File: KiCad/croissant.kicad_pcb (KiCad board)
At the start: 2 copper layers, 32 x 23 mm, 7 parts, among them J1 USB_C_Receptacle, U1 LMC555xM

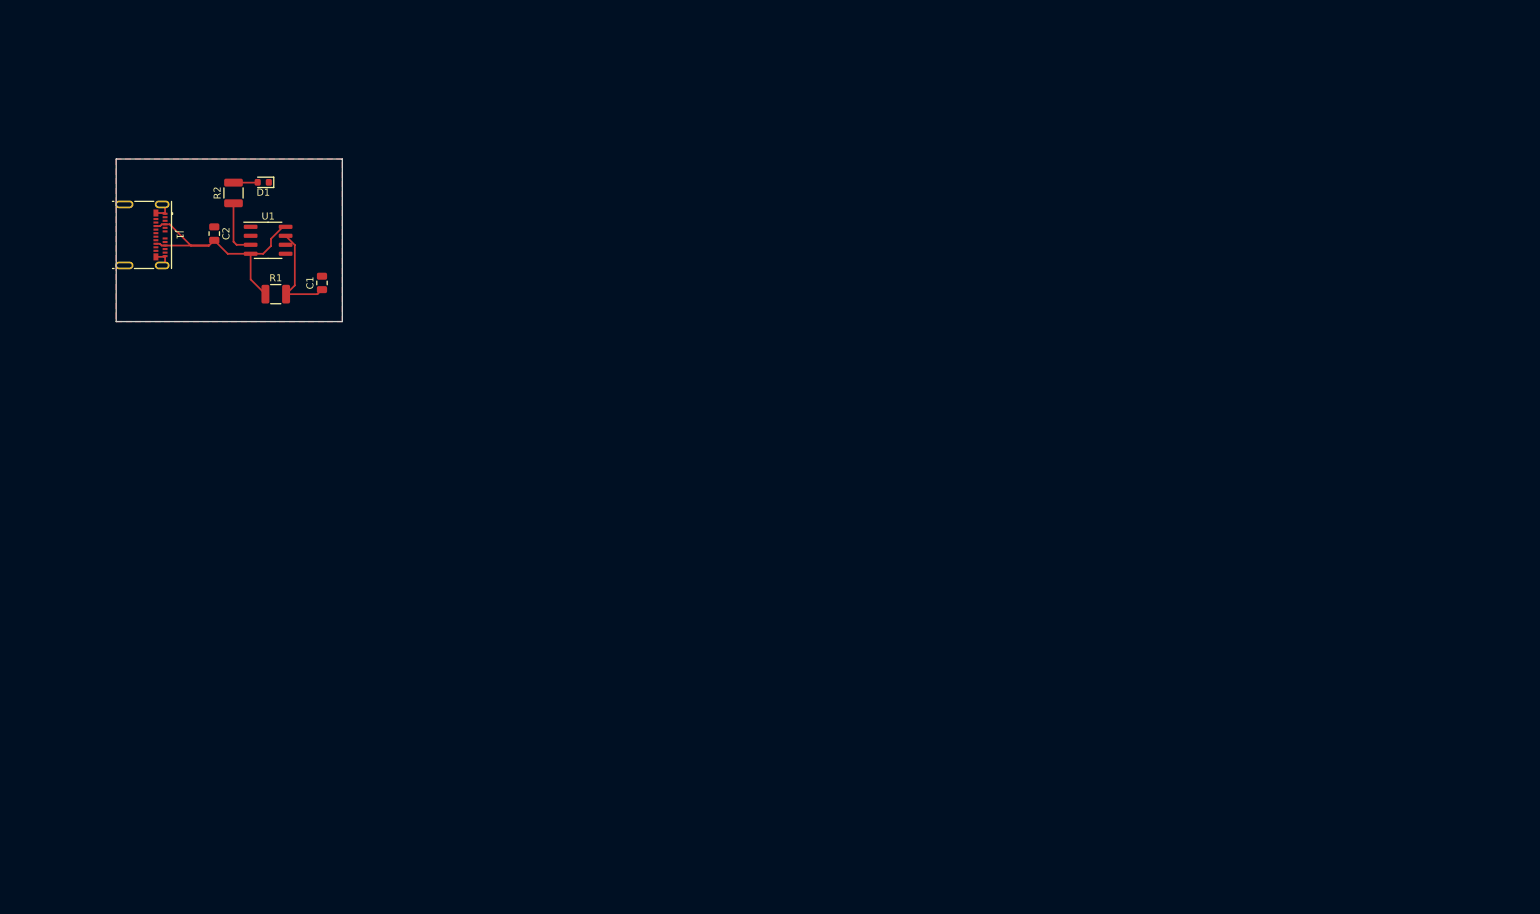
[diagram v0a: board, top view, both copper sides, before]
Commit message: Add board outline
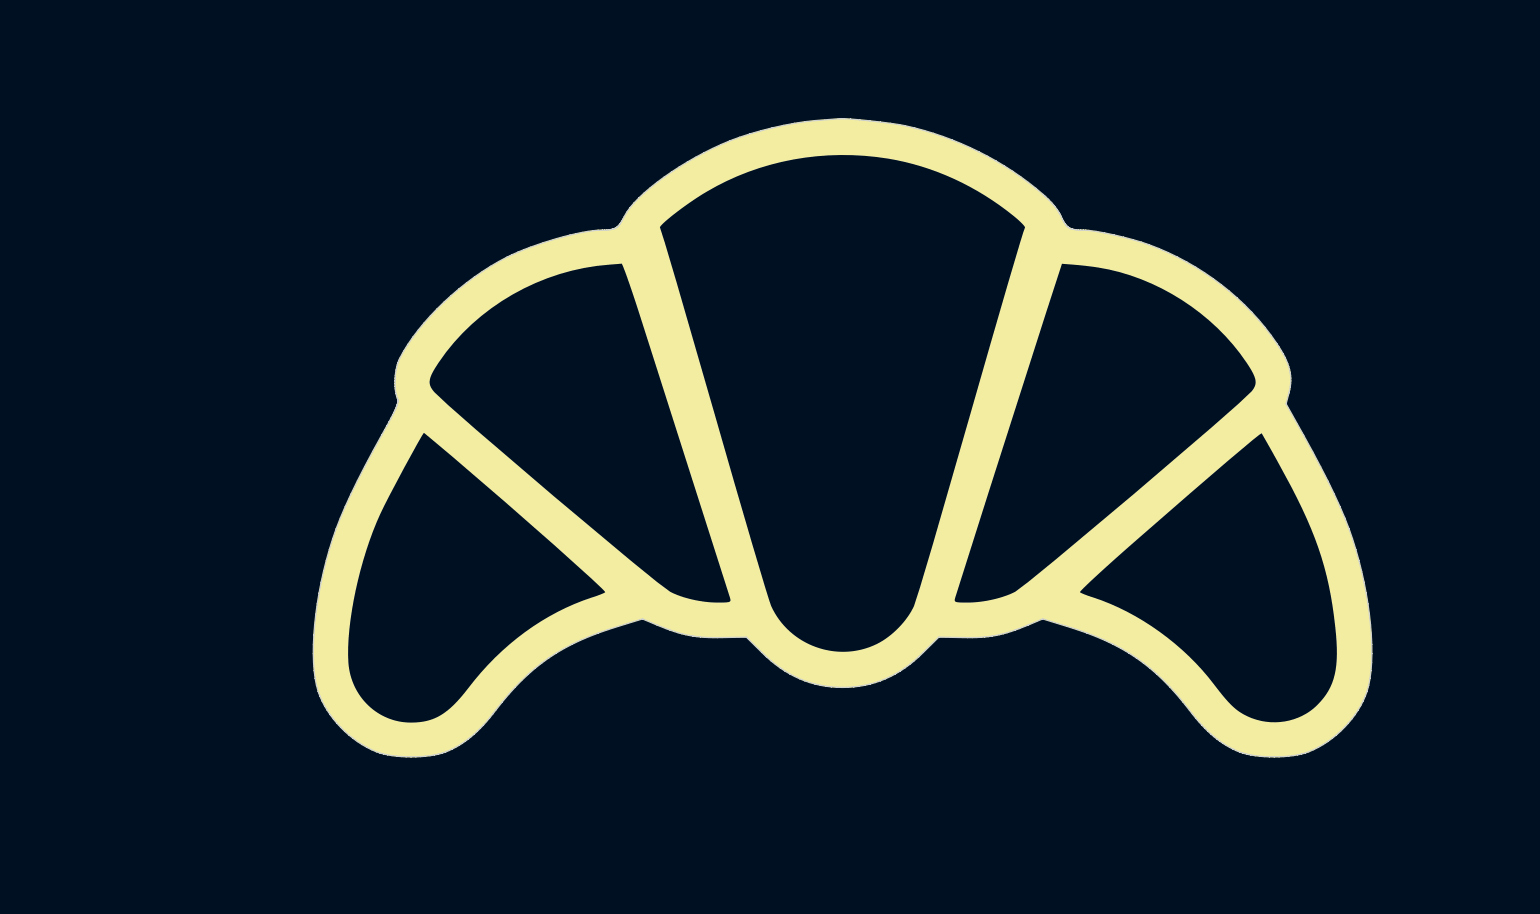
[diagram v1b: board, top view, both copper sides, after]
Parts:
- removed C1, C2: C, Capacitor_SMD:C_0805_2012Metric
- removed D1: LED, LED_SMD:LED_0603_1608Metric
- removed J1: USB_C_Receptacle, Connector_USB:USB_C_Receptacle_Molex_105450-0101
- removed R1, R2: R, Resistor_SMD:R_1210_3225Metric
- removed U1: LMC555xM, Package_SO:SOIC-8_3.9x4.9mm_P1.27mm
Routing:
- net +5V: track 37.2 -> 0.00 mm
- net Net-(U1-DIS): track 14.7 -> 0.00 mm
- net /555_output: track 8.04 -> 0.00 mm
- net GND: track 5.66 -> 0.00 mm
- net Net-(D1-A): track 3.44 -> 0.00 mm
- removed copper zone on F.Cu, net GND
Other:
- board size 32 x 23 mm -> 149.8 x 90.3 mm

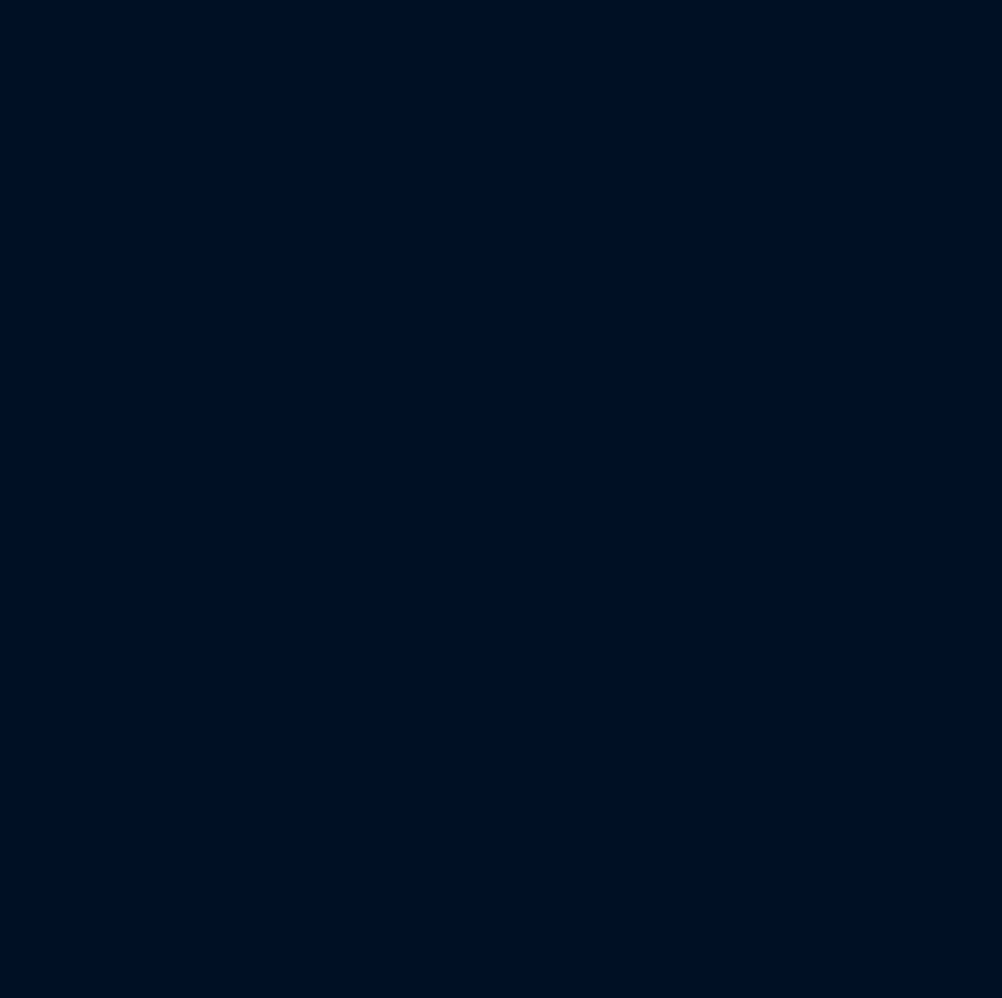
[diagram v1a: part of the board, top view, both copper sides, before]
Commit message: Fix footprints
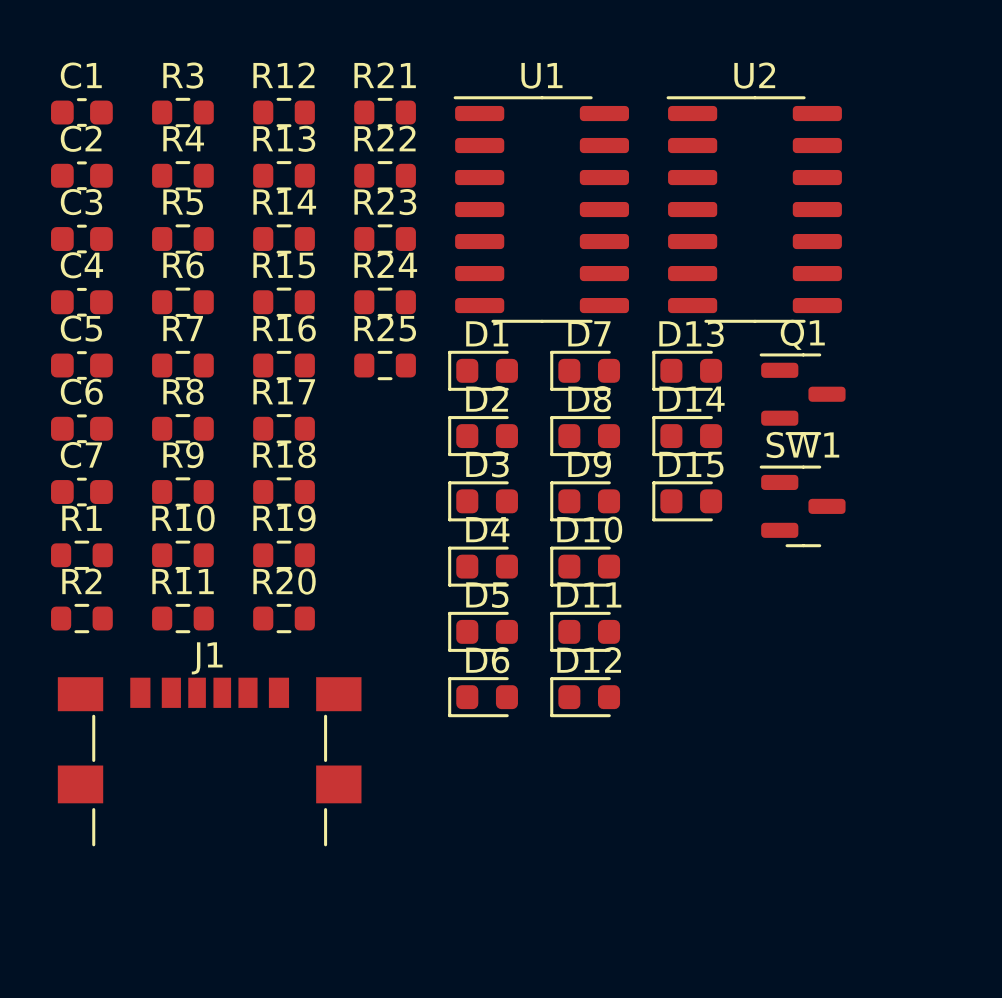
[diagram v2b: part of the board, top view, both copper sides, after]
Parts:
- added C1: C, Capacitor_SMD:C_0603_1608Metric, F.Cu at (51.7, 35.2)
- added C2: 22n, Capacitor_SMD:C_0603_1608Metric, F.Cu at (51.7, 37.7)
- added C3: 0.1u, Capacitor_SMD:C_0603_1608Metric, F.Cu at (51.7, 40.2)
- added C4: 0.1u, Capacitor_SMD:C_0603_1608Metric, F.Cu at (51.7, 42.7)
- added C5: 5n, Capacitor_SMD:C_0603_1608Metric, F.Cu at (51.7, 45.2)
- added C6: 1u, Capacitor_SMD:C_0603_1608Metric, F.Cu at (51.7, 47.7)
- added C7: 0.1u, Capacitor_SMD:C_0603_1608Metric, F.Cu at (51.7, 50.2)
- added D1: LED, LED_SMD:LED_0603_1608Metric, F.Cu at (67.8, 45.4)
- added D10: LED, LED_SMD:LED_0603_1608Metric, F.Cu at (71.8, 53.2)
- added D11: LED, LED_SMD:LED_0603_1608Metric, F.Cu at (71.8, 55.8)
- added D12: LED, LED_SMD:LED_0603_1608Metric, F.Cu at (71.8, 58.4)
- added D13: LED, LED_SMD:LED_0603_1608Metric, F.Cu at (75.9, 45.4)
- added D14: LED, LED_SMD:LED_0603_1608Metric, F.Cu at (75.9, 48.0)
- added D15: LED, LED_SMD:LED_0603_1608Metric, F.Cu at (75.9, 50.6)
- added D2: LED, LED_SMD:LED_0603_1608Metric, F.Cu at (67.8, 48.0)
- added D3: LED, LED_SMD:LED_0603_1608Metric, F.Cu at (67.8, 50.6)
- added D4: LED, LED_SMD:LED_0603_1608Metric, F.Cu at (67.8, 53.2)
- added D5: LED, LED_SMD:LED_0603_1608Metric, F.Cu at (67.8, 55.8)
- added D6: LED, LED_SMD:LED_0603_1608Metric, F.Cu at (67.8, 58.4)
- added D7: LED, LED_SMD:LED_0603_1608Metric, F.Cu at (71.8, 45.4)
- added D8: LED, LED_SMD:LED_0603_1608Metric, F.Cu at (71.8, 48.0)
- added D9: LED, LED_SMD:LED_0603_1608Metric, F.Cu at (71.8, 50.6)
- added J1: USB_C_Receptacle_PowerOnly_6P, Connector_USB:USB_C_Receptacle_GCT_USB4135-GF-A_6P_TopMnt_Horizontal, F.Cu at (56.8, 61.2)
- added Q1: NMOS, Package_TO_SOT_SMD:SOT-23, F.Cu at (80.3, 46.4)
- added R1: 18k, Resistor_SMD:R_0603_1608Metric, F.Cu at (51.7, 52.7)
- added R10: 1k, Resistor_SMD:R_0603_1608Metric, F.Cu at (55.7, 52.7)
- added R11: 1k, Resistor_SMD:R_0603_1608Metric, F.Cu at (55.7, 55.2)
- added R12: 1k, Resistor_SMD:R_0603_1608Metric, F.Cu at (59.7, 35.2)
- added R13: 1k, Resistor_SMD:R_0603_1608Metric, F.Cu at (59.7, 37.7)
- added R14: 1k, Resistor_SMD:R_0603_1608Metric, F.Cu at (59.7, 40.2)
- added R15: 1k, Resistor_SMD:R_0603_1608Metric, F.Cu at (59.7, 42.7)
- added R16: 1k, Resistor_SMD:R_0603_1608Metric, F.Cu at (59.7, 45.2)
- added R17: 1k, Resistor_SMD:R_0603_1608Metric, F.Cu at (59.7, 47.7)
- added R18: 1k, Resistor_SMD:R_0603_1608Metric, F.Cu at (59.7, 50.2)
- added R19: 1k, Resistor_SMD:R_0603_1608Metric, F.Cu at (59.7, 52.7)
- added R2: 82k, Resistor_SMD:R_0603_1608Metric, F.Cu at (51.7, 55.2)
- added R20: 1k, Resistor_SMD:R_0603_1608Metric, F.Cu at (59.7, 55.2)
- added R21: 1k, Resistor_SMD:R_0603_1608Metric, F.Cu at (63.7, 35.2)
- added R22: 1k, Resistor_SMD:R_0603_1608Metric, F.Cu at (63.7, 37.7)
- added R23: 1k, Resistor_SMD:R_0603_1608Metric, F.Cu at (63.7, 40.2)
- added R24: 0, Resistor_SMD:R_0603_1608Metric, F.Cu at (63.7, 42.7)
- added R25: 0, Resistor_SMD:R_0603_1608Metric, F.Cu at (63.7, 45.2)
- added R3: 10k, Resistor_SMD:R_0603_1608Metric, F.Cu at (55.7, 35.2)
- added R4: 10k, Resistor_SMD:R_0603_1608Metric, F.Cu at (55.7, 37.7)
- added R5: 100k, Resistor_SMD:R_0603_1608Metric, F.Cu at (55.7, 40.2)
- added R6: 6k8, Resistor_SMD:R_0603_1608Metric, F.Cu at (55.7, 42.7)
- added R7: 4k7, Resistor_SMD:R_0603_1608Metric, F.Cu at (55.7, 45.2)
- added R8: 680k, Resistor_SMD:R_0603_1608Metric, F.Cu at (55.7, 47.7)
- added R9: 1k, Resistor_SMD:R_0603_1608Metric, F.Cu at (55.7, 50.2)
- added SW1: SW_SPST, Package_TO_SOT_SMD:SOT-23, F.Cu at (80.3, 50.8)
- added U1: NE556, Package_SO:SOIC-14_3.9x8.7mm_P1.27mm, F.Cu at (70.0, 39.0)
- added U2: TL064, Package_SO:SOIC-14_3.9x8.7mm_P1.27mm, F.Cu at (78.4, 39.0)

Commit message: Add SPDT footprint
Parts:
- added C8: 10u, Capacitor_SMD:CP_Elec_4x3, F.Cu at (79.5, 58.4)
- R8: value 680k -> 4Meg
- SW1: value SW_SPST -> SW_SPDT; footprint Package_TO_SOT_SMD:SOT-23 -> croissant:JS102011JCQN
- moved SW1 6.61 mm to (86.4, 53.3)
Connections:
- J1 pad A9: Net-(SW1-A) -> Net-(SW1-B)
- J1 pad B9: Net-(SW1-A) -> Net-(SW1-B)
- SW1 pad 1: Net-(SW1-A) -> +5V
- SW1 pad 2: +5V -> Net-(SW1-B)
- SW1 pad 3: (no net) -> unconnected-(SW1-C-Pad3)

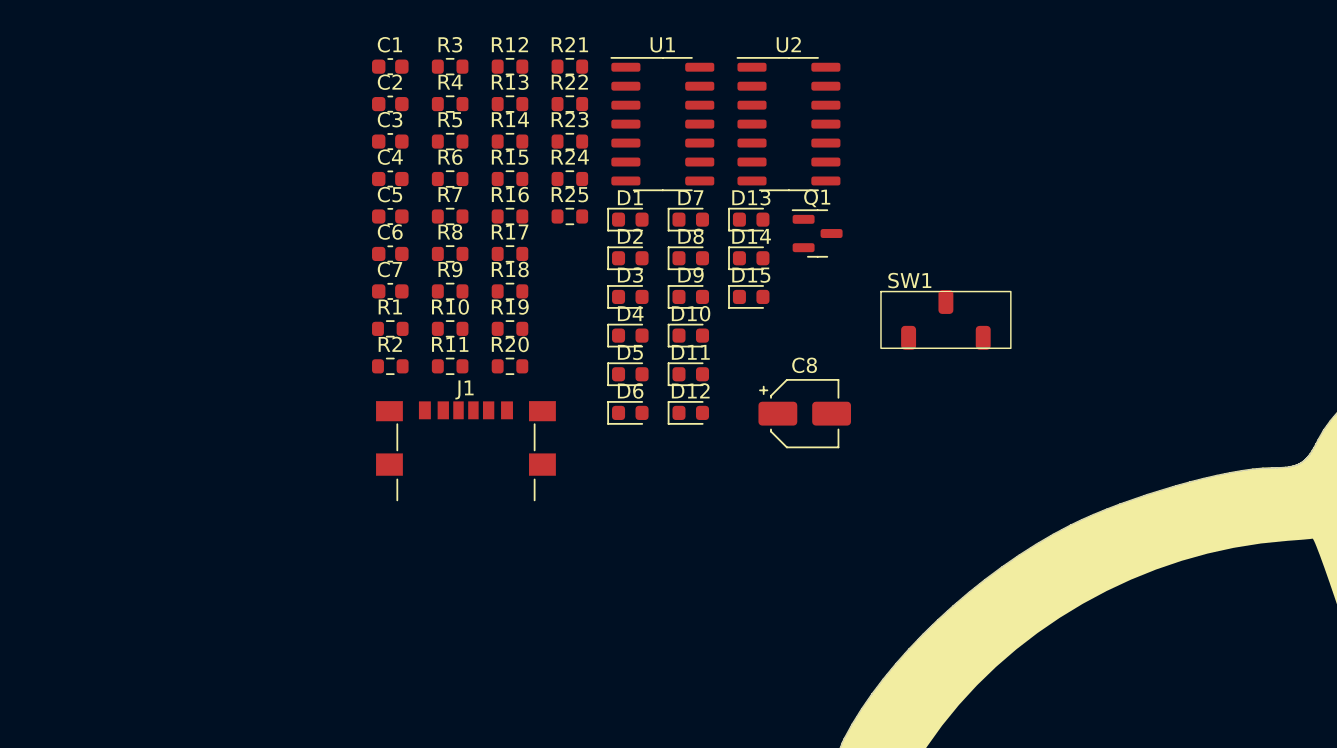
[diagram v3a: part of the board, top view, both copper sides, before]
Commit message: Fix JLCPCB stackup
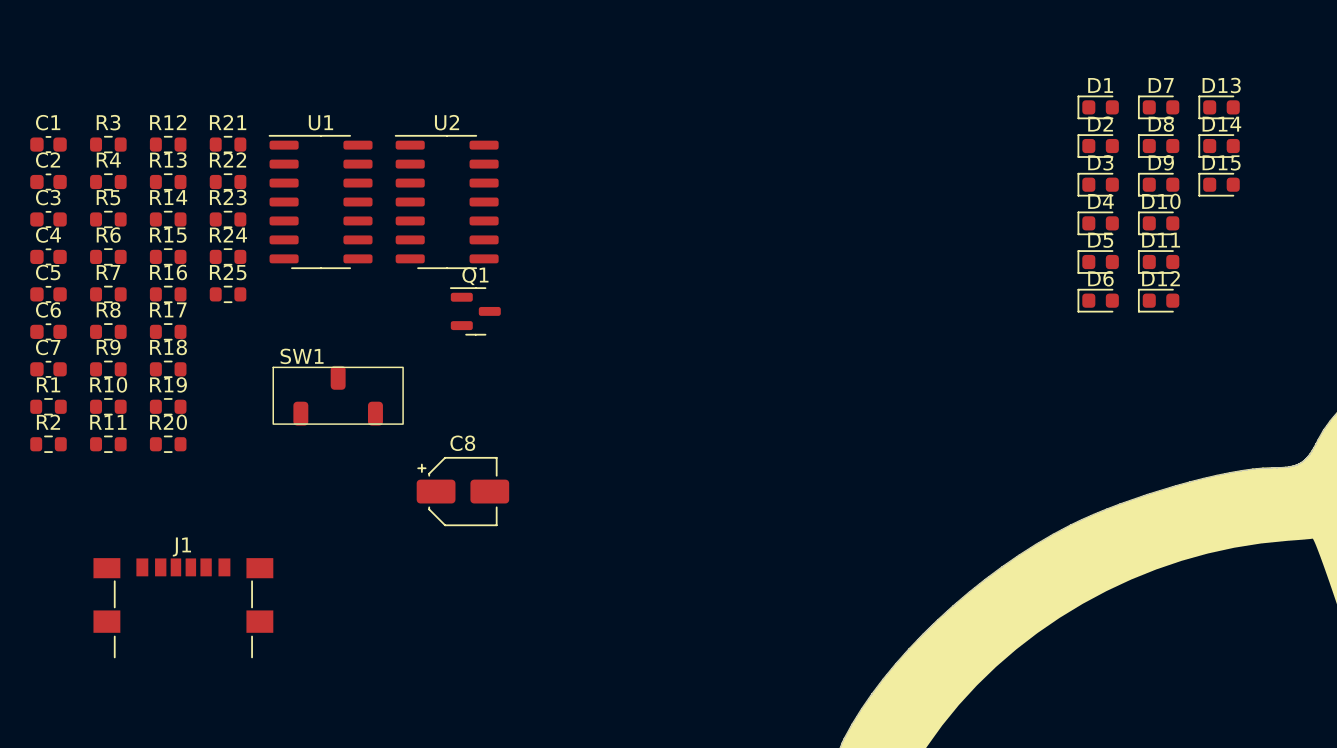
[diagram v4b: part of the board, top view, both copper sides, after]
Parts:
- moved SW1 41.0 mm to (45.7, 58.4)
- moved D10 32.4 mm to (103.4, 45.7)
- moved D11 32.4 mm to (103.4, 48.3)
- moved D12 32.4 mm to (103.4, 50.9)
- moved D13 32.4 mm to (107.4, 37.9)
- moved D14 32.4 mm to (107.4, 40.5)
- moved D15 32.4 mm to (107.4, 43.1)
- moved D7 32.4 mm to (103.4, 37.9)
- moved D8 32.4 mm to (103.4, 40.5)
- moved D9 32.4 mm to (103.4, 43.1)
- moved D1 32.4 mm to (99.3, 37.9)
- moved D2 32.4 mm to (99.3, 40.5)
- moved D3 32.4 mm to (99.3, 43.1)
- moved D4 32.4 mm to (99.3, 45.7)
- moved D5 32.4 mm to (99.3, 48.3)
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
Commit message: Advance routing
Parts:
- C1: value C -> 0.1u; moved to B.Cu
- C2, C3, C4, C5, C6, C7, C8, J1, Q1, R1, R10, R11, R12, R13, R14, R15, R16, R17, R18, R19, R2, R20, R21, R22, R23, R24, R25, R3, R4, R5, R6, R7, R8, R9, SW1, U1, U2: moved to B.Cu
- moved R10 189.9 mm to (222.7, 55.3), turned to 180 degrees
- moved R11 189.9 mm to (222.7, 57.8), turned to 180 degrees
- moved R9 189.9 mm to (222.7, 52.8), turned to 180 degrees
- moved R12 181.9 mm to (218.7, 37.7), turned to 180 degrees
- moved R13 181.9 mm to (218.7, 40.2), turned to 180 degrees
- moved R14 181.9 mm to (218.7, 42.7), turned to 180 degrees
- moved R15 181.9 mm to (218.7, 45.2), turned to 180 degrees
- moved R16 181.9 mm to (218.7, 47.8), turned to 180 degrees
- moved R17 181.9 mm to (218.7, 50.3), turned to 180 degrees
- moved R18 181.9 mm to (218.7, 52.8), turned to 180 degrees
- moved R19 181.9 mm to (218.7, 55.3), turned to 180 degrees
- moved R20 181.9 mm to (218.7, 57.8), turned to 180 degrees
- moved R21 173.8 mm to (214.7, 37.7), turned to 180 degrees
- moved R22 173.8 mm to (214.7, 40.2), turned to 180 degrees
- moved R23 173.8 mm to (214.7, 42.7), turned to 180 degrees
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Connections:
- C4 pad 1: +5V -> GND
- C4 pad 2: GND -> Net-(U1A-CV)
- U1 pad 3: unconnected-(U1A-CV-Pad3) -> Net-(U1A-CV)
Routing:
- net +5V: track 0.00 -> 152.0 mm
- net Net-(Q1-G): track 0.00 -> 21.9 mm
- net /PulseOut: track 0.00 -> 14.4 mm
- net Net-(U1B-DIS): track 0.00 -> 11.7 mm
- net Net-(U1A-THR): track 0.00 -> 10.8 mm
- net Net-(SW1-B): track 0.00 -> 9.33 mm
- net Net-(U1A-DIS): track 0.00 -> 9.13 mm
- net /PWMOut: track 0.00 -> 7.02 mm
- net Net-(U1A-CV): track 0.00 -> 3.15 mm
- added copper zone on B.Cu, net GND
